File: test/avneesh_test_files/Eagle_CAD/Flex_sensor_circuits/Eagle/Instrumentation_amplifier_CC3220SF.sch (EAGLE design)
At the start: 9 parts, among them IC1 LM324N, IC2 4051N

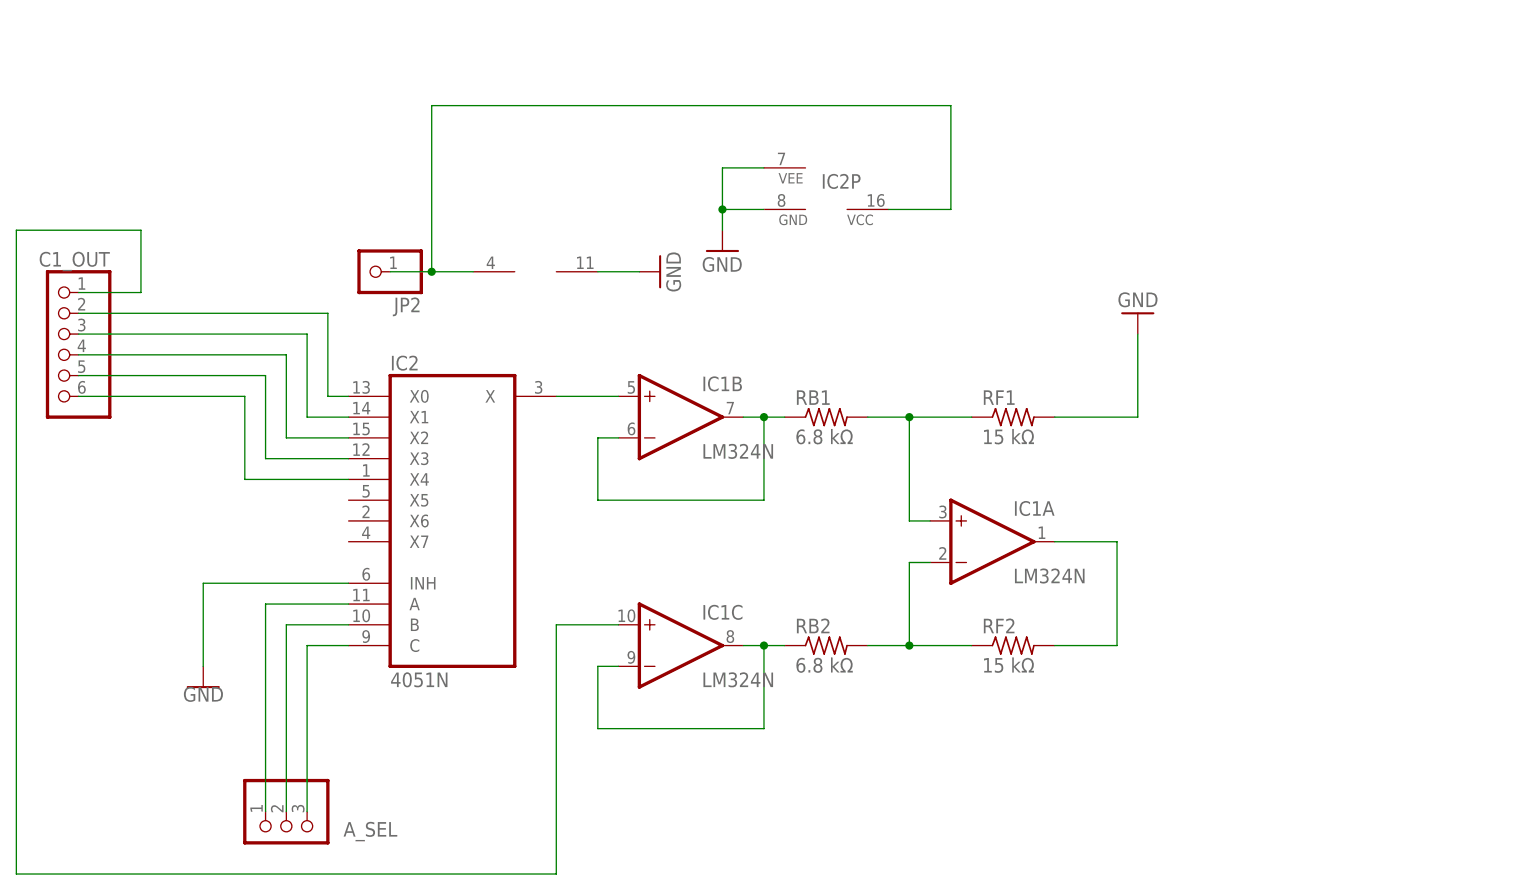
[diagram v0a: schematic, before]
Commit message: Added isntrumentation amplifier CAD files and board files
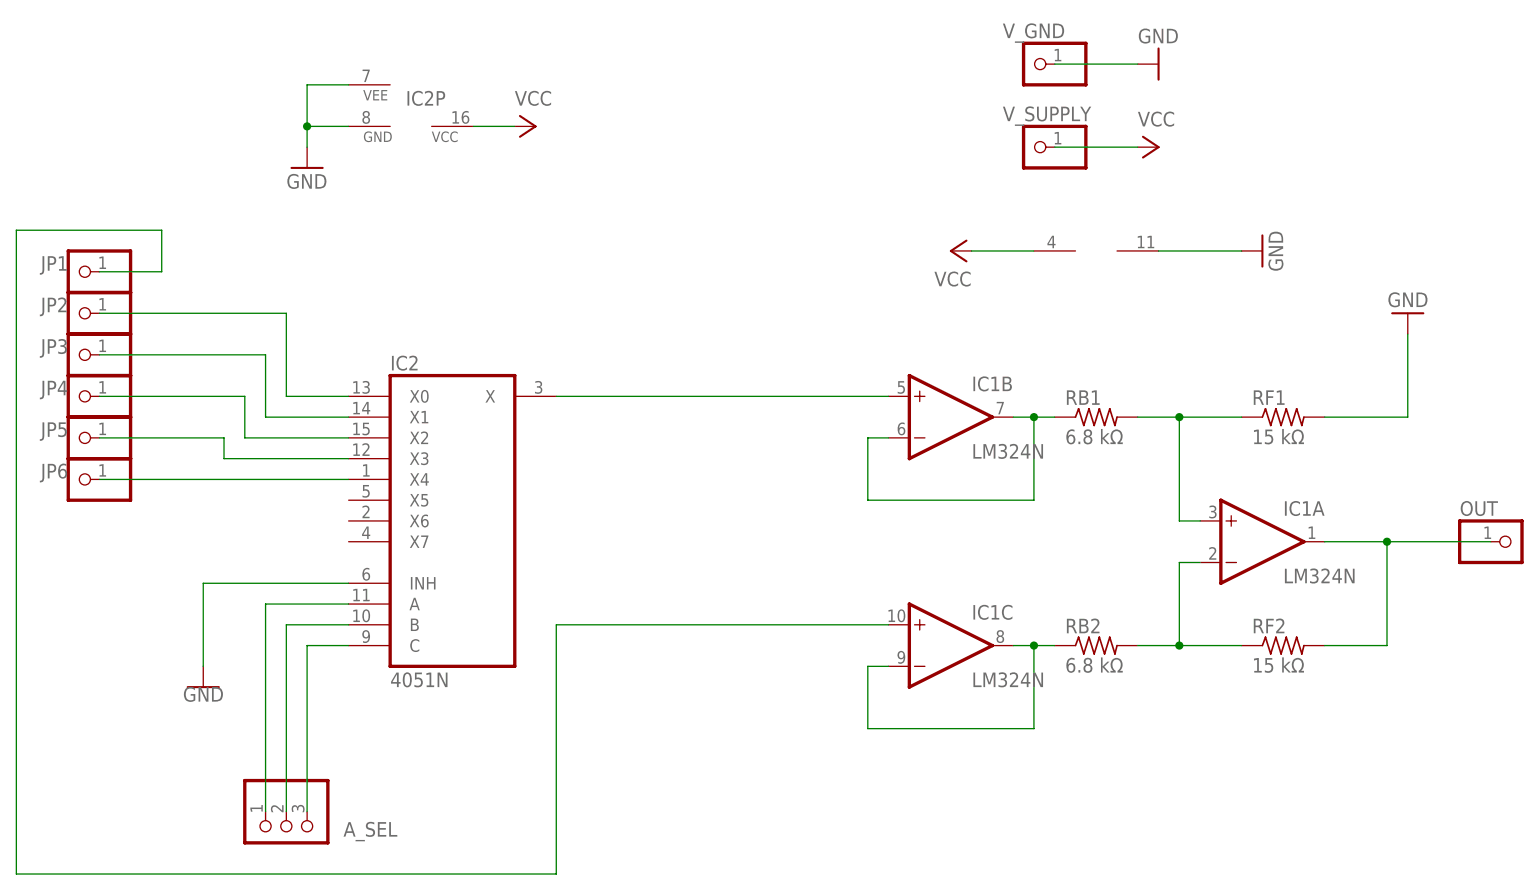
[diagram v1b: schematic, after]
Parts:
- removed C1_OUT: (no value), pinhead:PINHD-1X6
- added JP1, JP3, JP4, JP5, JP6, OUT, V_GND, V_SUPPLY: (no value), pinhead:PINHD-1X1
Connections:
- removed net N$7 (its old number): IC1A.OUT, RF2.2
- new net VCC: IC1P.V+, IC2P.VCC, V_SUPPLY.1
- net GND: now also V_GND.1
- net N$1: now also JP1.1; no longer C1_OUT.1
- net N$10: now also IC1A.OUT, OUT.1, RF2.2; no longer IC1P.V+, IC2P.VCC, JP2.1
- net N$12: now also JP5.1; no longer C1_OUT.5
- net N$13: now also JP6.1; no longer C1_OUT.6
- net N$6: now also JP2.1; no longer C1_OUT.2
- net N$8: now also JP3.1; no longer C1_OUT.3
- net N$9: now also JP4.1; no longer C1_OUT.4
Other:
- moved on the sheet: IC1A, IC1B, IC1C, IC2P, JP2, RB1, RB2, RF1, RF2
